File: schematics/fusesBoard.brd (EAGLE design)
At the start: 22 parts, among them Q1 IRF540, Q2 IRF540, Q3 IRF540

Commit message: made on earth
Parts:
- moved R7 16.3 mm to (44.8, 28.4), turned to 0 degrees
- moved R6 8.75 mm to (13.0, 28.4), turned to 0 degrees
- moved R4 3.83 mm to (13.3, 51.2)
- moved JP5 2.06 mm to (34.0, 5.61)
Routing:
- net GND: track 17.1 -> 44.5 mm
- net GATE3: track 38.4 -> 14.6 mm
- net N$1: track 22.3 -> 0.00 mm
- net CTRL3: track 22.6 -> 20.1 mm
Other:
- board text added: "Made on Earth by Granum"
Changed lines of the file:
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@@
 <hole x="45.04" y="37.05" drill="3"/>
 <hole x="45.04" y="43.11" drill="3"/>
+<text x="22.82" y="19.94" size="1.9304" layer="1" font="vector" ratio="17" align="center">Made on Earth
+by Granum</text>
 </plain>
 <attributes>
@@
 <element name="JP3" library="pinhead" package="1X01" value="" x="40.53" y="72.1"/>
 <element name="JP4" library="pinhead" package="1X01" value="" x="49.87" y="72.48"/>
-<element name="JP5" library="pinhead" package="1X01" value="" x="33.03" y="3.78"/>
+<element name="JP5" library="pinhead" package="1X01" value="" x="33.97" y="5.61"/>
 <element name="JP6" library="pinhead" package="1X01" value="" x="67.05" y="18.51"/>
 <element name="JP7" library="pinhead" package="1X01" value="" x="73.31" y="25.69"/>
@@
 <element name="R1" library="resistor" package="0204/7" value="10000" x="67.58" y="55.57" rot="R180"/>
 <element name="R2" library="resistor" package="0204/7" value="50" x="13.28" y="57.63"/>
-<element name="R4" library="resistor" package="0204/7" value="50" x="13.27" y="55.074"/>
-<element name="R6" library="resistor" package="0204/7" value="10000" x="20.44" y="23.91" rot="R90"/>
-<element name="R7" library="resistor" package="0204/7" value="10000" x="31.49" y="19.16" rot="R90"/>
+<element name="R4" library="resistor" package="0204/7" value="50" x="13.27" y="51.244"/>
+<element name="R6" library="resistor" package="0204/7" value="10000" x="12.96" y="28.45"/>
+<element name="R7" library="resistor" package="0204/7" value="10000" x="44.84" y="28.45"/>
 <element name="R9" library="resistor" package="0204/7" value="50" x="47.4" y="10.59"/>
 <element name="Q1" library="transistor-power" package="TO220BV" value="IRF540" x="55.7" y="57.15" rot="R270"/>
@@
 <contactref element="R7" pad="2"/>
 <contactref element="Q3" pad="G"/>
-<wire x1="48.66" y1="22.91" x2="48.66" y2="31.05" width="0.6096" layer="1"/>
-<wire x1="48.66" y1="31.05" x2="56.6" y2="31.05" width="0.6096" layer="1"/>
-<wire x1="48.66" y1="22.91" x2="48.66" y2="26.56" width="0.4064" layer="1"/>
-<wire x1="48.66" y1="26.56" x2="35.08" y2="26.56" width="0.6096" layer="1"/>
-<wire x1="35.08" y1="26.56" x2="31.49" y2="22.97" width="0.6096" layer="1"/>
+<wire x1="48.66" y1="22.91" x2="48.65" y2="22.91" width="0.6096" layer="1"/>
+<wire x1="48.65" y1="22.91" x2="48.65" y2="28.45" width="0.6096" layer="1"/>
+<wire x1="48.65" y1="28.45" x2="51.78" y2="28.45" width="0.6096" layer="1"/>
+<wire x1="51.78" y1="28.45" x2="54.41" y2="31.08" width="0.6096" layer="1"/>
+<wire x1="54.41" y1="31.08" x2="56.57" y2="31.08" width="0.6096" layer="1"/>
+<wire x1="56.57" y1="31.08" x2="56.6" y2="31.05" width="0.6096" layer="1"/>
 </signal>
 <signal name="N$18">
@@
 <wire x1="26.25" y1="45.75" x2="14.65" y2="45.75" width="0.6096" layer="1"/>
 <wire x1="14.65" y1="45.75" x2="14.65" y2="31.08" width="0.6096" layer="1"/>
-<wire x1="14.65" y1="31.08" x2="20.44" y2="31.08" width="0.6096" layer="1"/>
-<wire x1="20.44" y1="31.08" x2="27.08" y2="31.08" width="0.6096" layer="1"/>
-<wire x1="20.44" y1="27.72" x2="20.44" y2="31.08" width="0.6096" layer="1"/>
+<wire x1="14.65" y1="31.08" x2="17.08" y2="31.08" width="0.6096" layer="1"/>
+<wire x1="17.08" y1="31.08" x2="27.08" y2="31.08" width="0.6096" layer="1"/>
 <wire x1="29.78" y1="50.76" x2="29.78" y2="49.28" width="0.6096" layer="1"/>
 <wire x1="29.78" y1="49.28" x2="26.25" y2="45.75" width="0.6096" layer="1"/>
+<wire x1="16.77" y1="28.45" x2="17.08" y2="28.45" width="0.4064" layer="1"/>
+<wire x1="17.08" y1="28.45" x2="17.08" y2="31.08" width="0.6096" layer="1"/>
 </signal>
 <signal name="SOURCE2">
@@
 <contactref element="U$1" pad="3"/>
 <contactref element="R4" pad="2"/>
-<wire x1="17.08" y1="55.074" x2="18.854" y2="53.3" width="1.016" layer="1"/>
+<wire x1="17.08" y1="51.244" x2="18.854" y2="53.3" width="1.016" layer="1"/>
 <wire x1="18.854" y1="53.3" x2="22.16" y2="53.3" width="1.016" layer="1"/>
 </signal>
@@
 <contactref element="JP5" pad="1"/>
 <contactref element="U$2" pad="1"/>
-<wire x1="48.66" y1="15.29" x2="39.03" y2="15.28" width="1.016" layer="1"/>
-<wire x1="39.03" y1="15.28" x2="33.03" y2="3.78" width="1.016" layer="1"/>
+<wire x1="33.97" y1="5.61" x2="33.97" y2="7.97" width="0.6096" layer="1"/>
+<wire x1="33.97" y1="7.97" x2="41.37" y2="15.37" width="0.6096" layer="1"/>
+<wire x1="41.37" y1="15.37" x2="48.58" y2="15.37" width="0.6096" layer="1"/>
+<wire x1="48.58" y1="15.37" x2="48.66" y2="15.29" width="0.6096" layer="1"/>
 </signal>
 <signal name="GND">
@@
 <contactref element="R7" pad="1"/>
 <contactref element="R9" pad="1"/>
-<polygon width="1.016" layer="1" isolate="1.4224">
+<polygon width="1.016" layer="1" isolate="1.4224" orphans="yes">
 <vertex x="3.42" y="40.51" curve="-90"/>
 <vertex x="44.98" y="82.07"/>
@@
 <contactref element="Q2" pad="S"/>
 <contactref element="LSP1" pad="MP"/>
-<via x="64.08" y="26.63" extent="1-16" drill="1.4" shape="square"/>
-<via x="55.12" y="6.56" extent="1-16" drill="1.4" shape="square"/>
 <via x="58.89" y="53.33" extent="1-16" drill="1.4" shape="square"/>
 <via x="75.68" y="52.62" extent="1-16" drill="1.4" shape="square"/>
 <wire x1="58.89" y1="53.33" x2="74.97" y2="53.33" width="1.4224" layer="16"/>
 <wire x1="74.97" y1="53.33" x2="75.68" y2="52.62" width="1.4224" layer="16"/>
-<wire x1="58.89" y1="53.33" x2="61.68" y2="31.05" width="0" layer="19" extent="1-1"/>
+<wire x1="58.89" y1="53.33" x2="61.68" y2="53.33" width="0.6096" layer="16"/>
+<via x="63.93" y="27.37" extent="1-16" drill="1.4" shape="square"/>
+<via x="73.02" y="48.23" extent="1-16" drill="1.4" shape="square"/>
+<wire x1="63.93" y1="27.37" x2="63.93" y2="39.14" width="1.6764" layer="16"/>
+<wire x1="63.93" y1="39.14" x2="73.02" y2="48.23" width="1.6764" layer="16"/>
 </signal>
 <signal name="VCC">
@@
 </signal>
 <signal name="N$1">
-<wire x1="64.32" y1="26.39" x2="55.06" y2="6.11" width="1.4224" layer="16"/>
 </signal>
 </signals>
 </board>
 </drawing>
+<compatibility>
+<note version="6.3" minversion="6.2.2" severity="warning">
+Since Version 6.2.2 text objects can contain more than one line,
+which will not be processed correctly with this version.
+</note>
+</compatibility>
 </eagle>

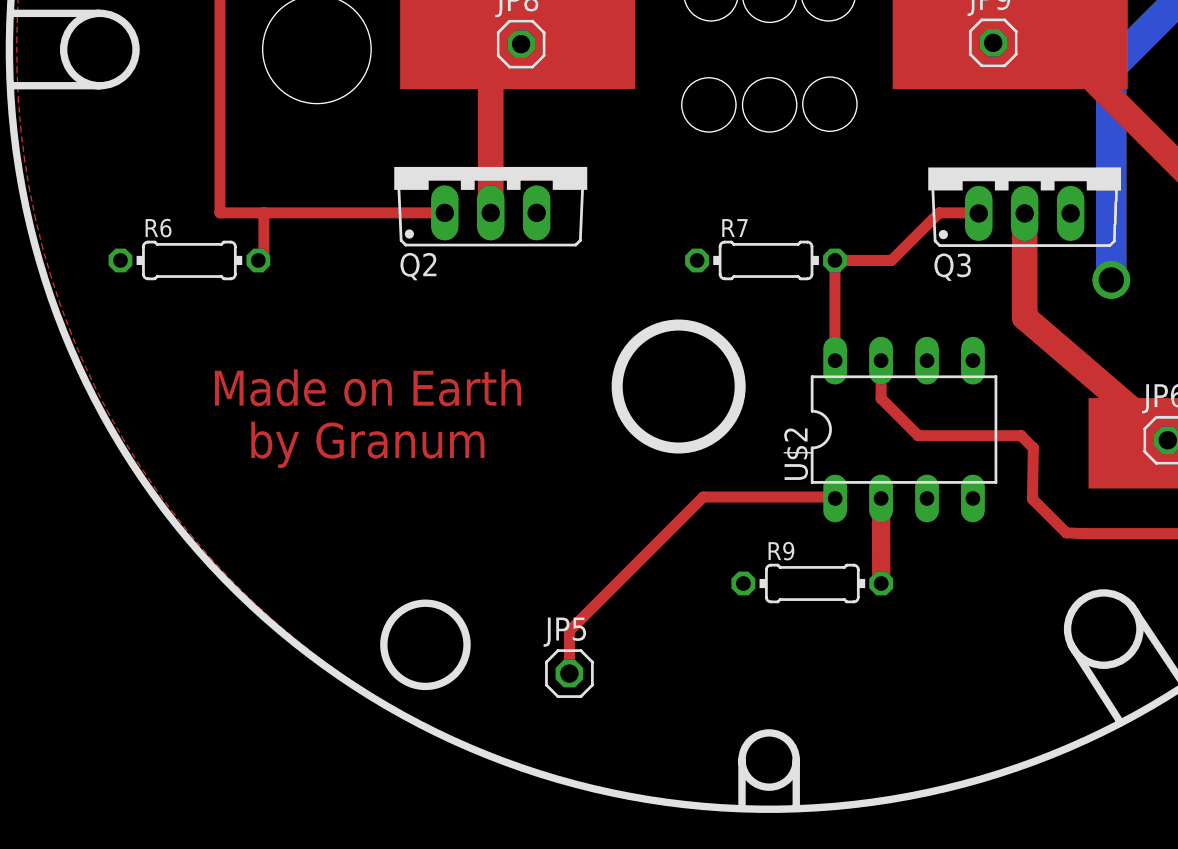
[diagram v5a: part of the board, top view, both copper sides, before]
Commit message: Поддержки для окошка для пережигателя и ремонт самого окошка
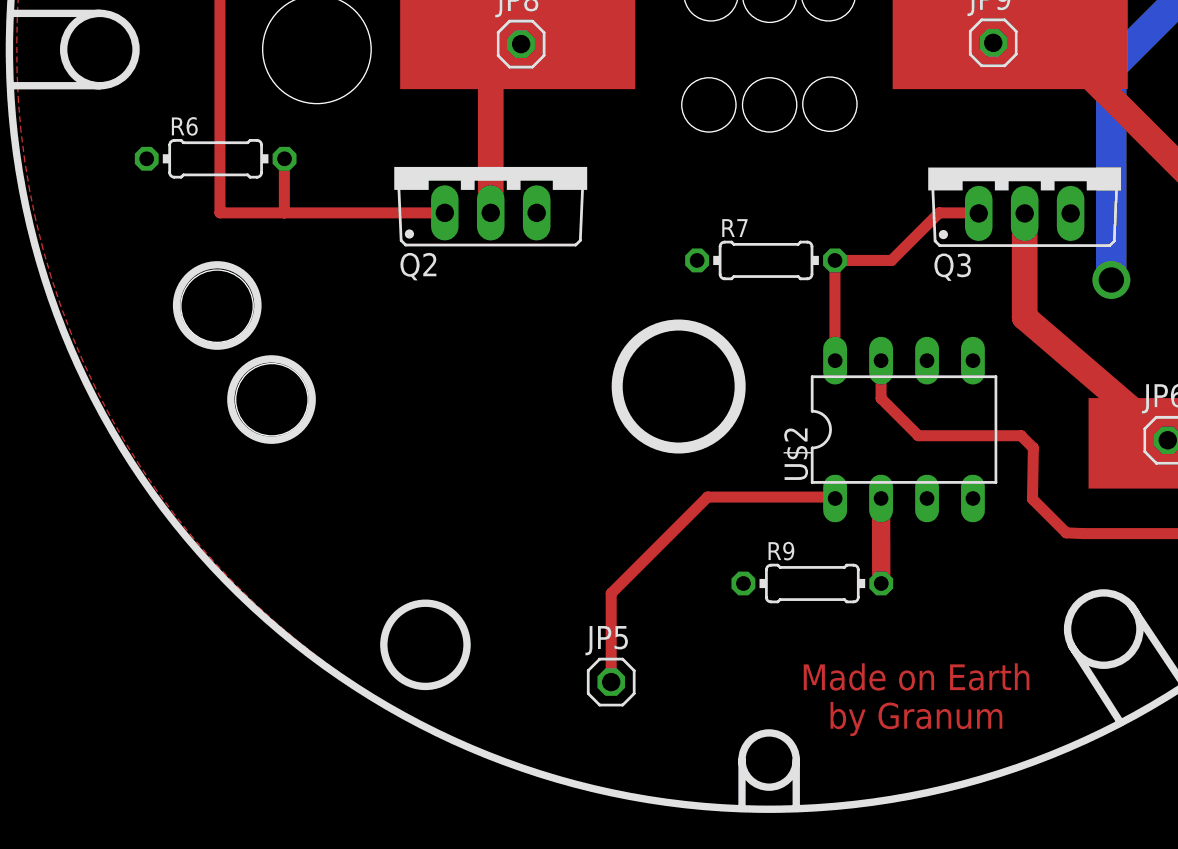
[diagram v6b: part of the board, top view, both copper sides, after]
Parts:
- moved R6 5.80 mm to (14.4, 34.1)
- moved JP5 2.36 mm to (36.3, 5.14)
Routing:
- net CTRL3: track 20.1 -> 19.5 mm
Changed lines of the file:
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@@
 <hole x="45.04" y="37.05" drill="3"/>
 <hole x="45.04" y="43.11" drill="3"/>
-<text x="22.82" y="19.94" size="1.9304" layer="1" font="vector" ratio="17" align="center">Made on Earth
+<text x="53.15" y="4.34" size="1.4224" layer="1" font="vector" ratio="17" align="center">Made on Earth
 by Granum</text>
+<circle x="17.5" y="20.76" radius="2.248040625" width="0.4064" layer="21"/>
+<circle x="14.5" y="25.96" radius="2.248040625" width="0.4064" layer="21"/>
+<hole x="14.49" y="25.92" drill="4"/>
+<hole x="17.52" y="20.75" drill="4"/>
 </plain>
 <attributes>
@@
 <element name="JP3" library="pinhead" package="1X01" value="" x="40.53" y="72.1"/>
 <element name="JP4" library="pinhead" package="1X01" value="" x="49.87" y="72.48"/>
-<element name="JP5" library="pinhead" package="1X01" value="" x="33.97" y="5.61"/>
+<element name="JP5" library="pinhead" package="1X01" value="" x="36.28" y="5.14"/>
 <element name="JP6" library="pinhead" package="1X01" value="" x="67.05" y="18.51"/>
 <element name="JP7" library="pinhead" package="1X01" value="" x="73.31" y="25.69"/>
@@
 <element name="R2" library="resistor" package="0204/7" value="50" x="13.28" y="57.63"/>
 <element name="R4" library="resistor" package="0204/7" value="50" x="13.27" y="51.244"/>
-<element name="R6" library="resistor" package="0204/7" value="10000" x="12.96" y="28.45"/>
+<element name="R6" library="resistor" package="0204/7" value="10000" x="14.41" y="34.07"/>
 <element name="R7" library="resistor" package="0204/7" value="10000" x="44.84" y="28.45"/>
 <element name="R9" library="resistor" package="0204/7" value="50" x="47.4" y="10.59"/>
@@
 <wire x1="26.25" y1="45.75" x2="14.65" y2="45.75" width="0.6096" layer="1"/>
 <wire x1="14.65" y1="45.75" x2="14.65" y2="31.08" width="0.6096" layer="1"/>
-<wire x1="14.65" y1="31.08" x2="17.08" y2="31.08" width="0.6096" layer="1"/>
-<wire x1="17.08" y1="31.08" x2="27.08" y2="31.08" width="0.6096" layer="1"/>
+<wire x1="14.65" y1="31.08" x2="18.21" y2="31.08" width="0.6096" layer="1"/>
+<wire x1="18.21" y1="31.08" x2="27.08" y2="31.08" width="0.6096" layer="1"/>
 <wire x1="29.78" y1="50.76" x2="29.78" y2="49.28" width="0.6096" layer="1"/>
 <wire x1="29.78" y1="49.28" x2="26.25" y2="45.75" width="0.6096" layer="1"/>
-<wire x1="16.77" y1="28.45" x2="17.08" y2="28.45" width="0.4064" layer="1"/>
-<wire x1="17.08" y1="28.45" x2="17.08" y2="31.08" width="0.6096" layer="1"/>
+<wire x1="18.22" y1="34.07" x2="18.21" y2="34.07" width="0.4064" layer="1"/>
+<wire x1="18.21" y1="34.07" x2="18.21" y2="31.08" width="0.6096" layer="1"/>
 </signal>
 <signal name="SOURCE2">
@@
 <contactref element="JP5" pad="1"/>
 <contactref element="U$2" pad="1"/>
-<wire x1="33.97" y1="5.61" x2="33.97" y2="7.97" width="0.6096" layer="1"/>
-<wire x1="33.97" y1="7.97" x2="41.37" y2="15.37" width="0.6096" layer="1"/>
-<wire x1="41.37" y1="15.37" x2="48.58" y2="15.37" width="0.6096" layer="1"/>
+<wire x1="41.61" y1="15.37" x2="48.58" y2="15.37" width="0.6096" layer="1"/>
 <wire x1="48.58" y1="15.37" x2="48.66" y2="15.29" width="0.6096" layer="1"/>
+<wire x1="36.28" y1="5.14" x2="36.28" y2="10.04" width="0.6096" layer="1"/>
+<wire x1="36.28" y1="10.04" x2="41.61" y2="15.37" width="0.6096" layer="1"/>
 </signal>
 <signal name="GND">
